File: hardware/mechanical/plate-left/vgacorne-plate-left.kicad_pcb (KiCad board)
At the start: 2 copper layers, 138.8 x 98 mm, 0 parts

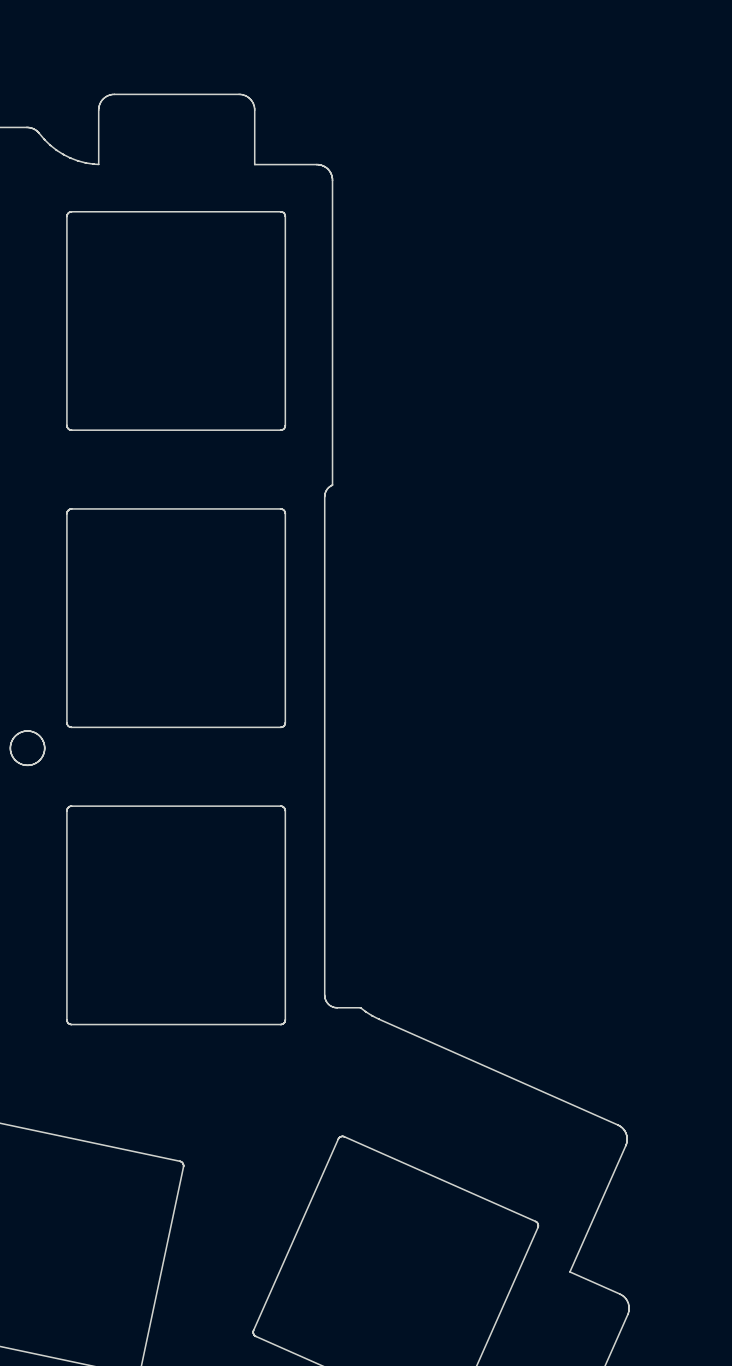
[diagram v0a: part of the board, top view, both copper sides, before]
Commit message: Add trackpad, mouse column and scroll wheel; move MCU and ports
Layout
- MCU module, USB-C and trackpad move to the right half; the left half
  is now the passive satellite.
- VGA daughterboard bay moves to the inner-back corner so both cables
  leave from the back face. The bay sits 4.5 mm further back than the
  keys need, so both halves are 116 mm deep.
- Azoteq TPS65 trackpad, landscape, right beside Y/H/N under a 1 mm
  overlay. The MCU module moves to a PCB ear behind it, next to the
  VGA bay. trackpad.py selects the pad (TPS65 or 40 mm Cirque); the
  case pocket, J5 connector and QMK driver follow the selection.
- Left half: a mouse column beside T/G/B with a scroll wheel (Bourns
  PEC12R) at the top and left/right-click HE keys beside G and B.

Circuits and firmware
- Mux channels reassigned so the satellite's mouse keys and wheel fill
  its three spare channels. The wheel's A/B contacts are summed into
  four voltage levels on one channel.
- QMK: 44-key LAYOUT and a wheel decoder that feeds QMK's quadrature
  encoder driver. Trackpad on I2C1, with rules.mk now generated. The
  host test covers the wheel.
- libhmk: MS_BTN1/MS_BTN2 on the mouse keys (no encoder support).

Case and renders
- Smoother milled case: 7.25 mm walls, 25 mm minimum outside radius
  and a flat back face at the ports.
- render.py builds Blender Cycles renders from the design geometry.

Co-Authored-By: Claude Opus 5.5 (1M context) <noreply@anthropic.com>
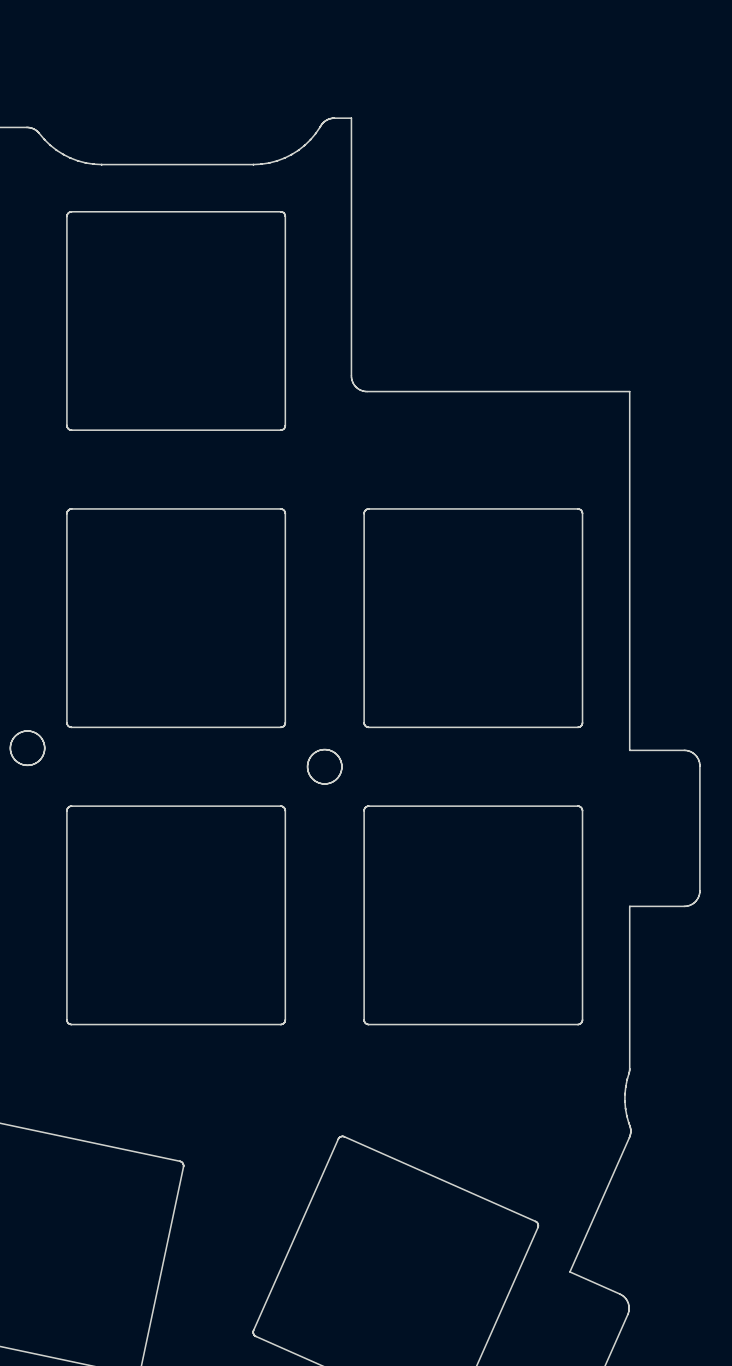
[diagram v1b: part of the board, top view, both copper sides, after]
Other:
- board size 138.8 x 98 mm -> 143.4 x 98 mm

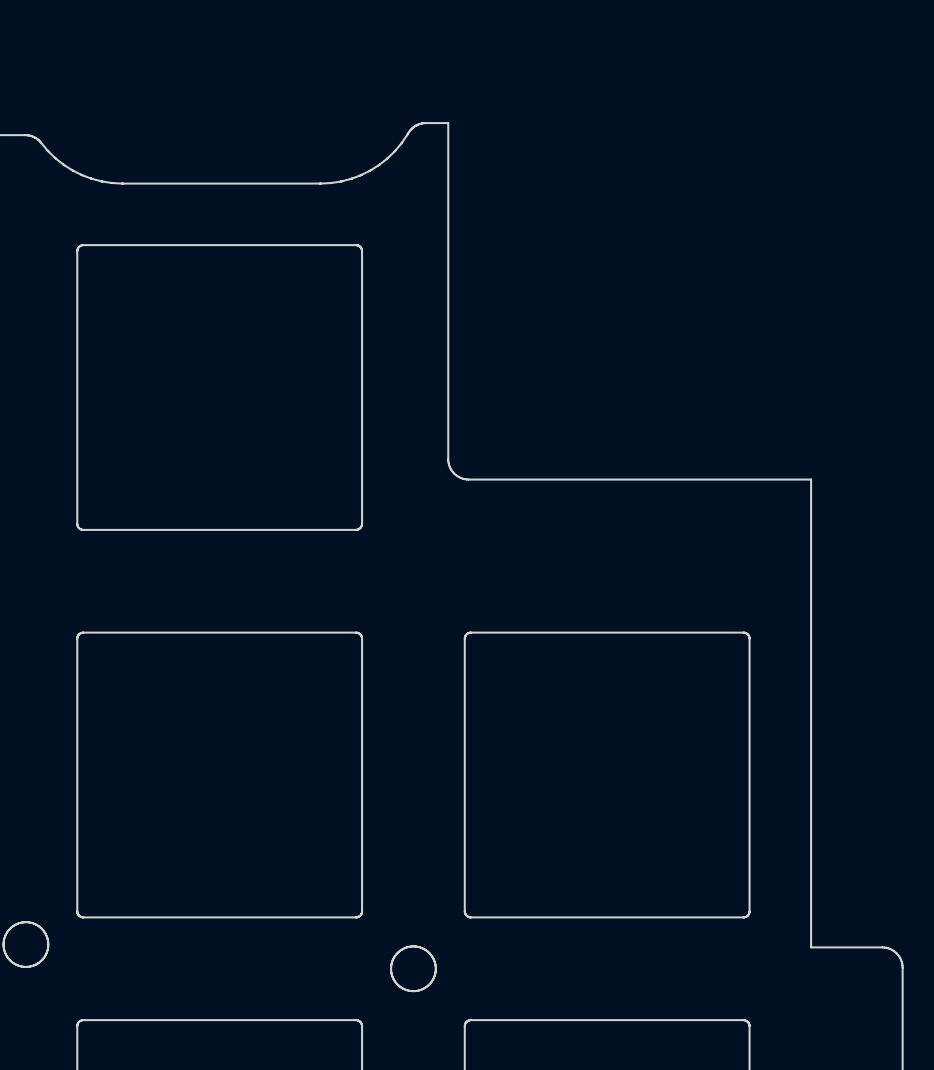
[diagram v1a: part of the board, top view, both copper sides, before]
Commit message: Replace the scroll wheel with a rotary encoder knob
The left half's mouse column now runs, top to bottom: right click beside
T, left click beside G, and a rotary encoder with a knob beside B, all
in line with column 5's rows.
- Encoder: Bourns PEC12R-4220F-N0024 (upright, 20 mm shaft, 24
  detents, no switch). It sits in a normal 14 mm plate cutout, which
  replaces the wheel notch. The knob is 16 mm across.
- Same readout as before: the A/B contacts are summed into four levels
  on the satellite's last spare mux channel. Nets, QMK defines and code
  are renamed from wheel to encoder (ENC, HE_ENCODER_*).
- The link connector J3 goes back to its original spot, now that the
  encoder legs are elsewhere.
- Docs, BOM, PCB images and renders regenerated.

Co-Authored-By: Claude Opus 5.5 (1M context) <noreply@anthropic.com>
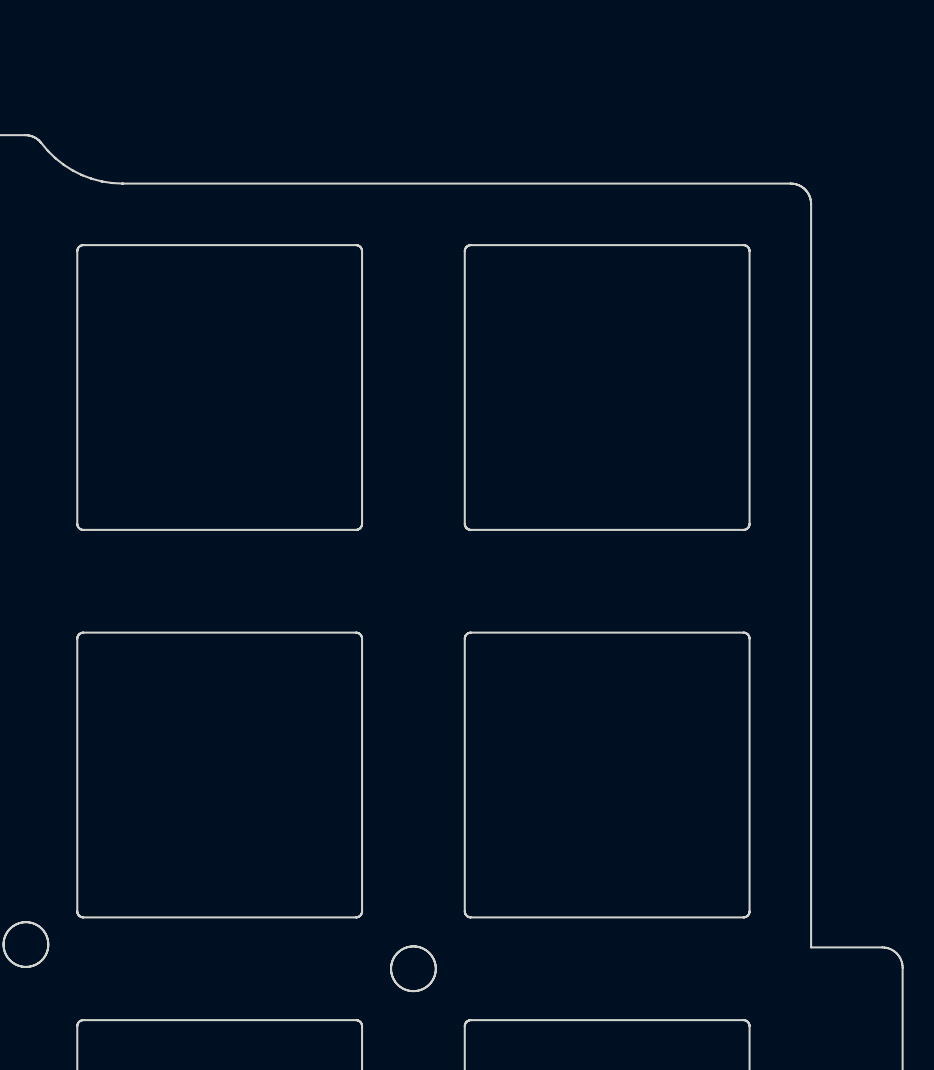
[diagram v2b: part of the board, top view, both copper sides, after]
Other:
- outline, holes or cut-outs redrawn
